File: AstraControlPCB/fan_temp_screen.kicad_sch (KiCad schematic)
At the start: 23 parts, among them CN4 4P JST ZH, CN5 4P JST ZH, CN6 4P JST ZH

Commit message: update
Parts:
- removed R26, R27, R33, R34: 0, LiveAstra:R_0805_2012Metric_Pad1.20x1.40mm_HandSolder, symbol LiveAstra:R_0Ohm_0805_125mW
- added R26, R27, R33, R34: DNP, LiveAstra:R_0805_2012Metric_Pad1.20x1.40mm_HandSolder, symbol LiveAstra:R_DNP_0805
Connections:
- net +3V3: now also R26.2, R27.2, R33.2, R34.2
- net SCREEN_I2C_SCL: now also R27.1
- net SCREEN_I2C_SDA: now also R34.1
- net TEMP_I2C_SCL: now also R26.1
- net TEMP_I2C_SDA: now also R33.1

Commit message: Fixed fab layer
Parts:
- R26, R27, R33, R34: footprint LiveAstra:R_0805_2012Metric_Pad1.20x1.40mm_HandSolder -> LiveAstra:R_DNP_0805_2012Metric_Pad1.20x1.40mm_HandSolder
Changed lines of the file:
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@@
 			)
 		)
-		(property "Footprint" "LiveAstra:R_0805_2012Metric_Pad1.20x1.40mm_HandSolder"
+		(property "Footprint" "LiveAstra:R_DNP_0805_2012Metric_Pad1.20x1.40mm_HandSolder"
 			(at 228.6 152.4 0)
 			(effects
@@
 			)
 		)
-		(property "Footprint" "LiveAstra:R_0805_2012Metric_Pad1.20x1.40mm_HandSolder"
+		(property "Footprint" "LiveAstra:R_DNP_0805_2012Metric_Pad1.20x1.40mm_HandSolder"
 			(at 137.16 96.52 0)
 			(effects
@@
 			)
 		)
-		(property "Footprint" "LiveAstra:R_0805_2012Metric_Pad1.20x1.40mm_HandSolder"
+		(property "Footprint" "LiveAstra:R_DNP_0805_2012Metric_Pad1.20x1.40mm_HandSolder"
 			(at 228.6 101.6 0)
 			(effects
@@
 			)
 		)
-		(property "Footprint" "LiveAstra:R_0805_2012Metric_Pad1.20x1.40mm_HandSolder"
+		(property "Footprint" "LiveAstra:R_DNP_0805_2012Metric_Pad1.20x1.40mm_HandSolder"
 			(at 137.16 147.32 0)
 			(effects

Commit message: Updates
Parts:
- renumbered C22 to C23, INF6 to INF8, R23 to R24, R24 to R25, R25 to R26, R26 to R27, R27 to R28, R28 to R29, R29 to R30, R30 to R31, R31 to R32, R32 to R33, R33 to R34, R34 to R35

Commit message: Added MFN MPR to each components for eurocircuits
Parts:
- C23: MFN (none) -> Samsung Electro-Mechanics; MPN (none) -> CL21C101JBANNNC
- CN4, CN5, CN6: MFN (none) -> JST; MPN (none) -> B4B-ZR-3.4(LF)(SN)
- R24, R25, R32, R33: MFN (none) -> UNI-ROYAL(Uniroyal Elec); MPN (none) -> 0402WGF5101TCE
- R26, R29: MFN (none) -> UNI-ROYAL(Uniroyal Elec); MPN (none) -> 0805W8F0000T5E
- R30: MFN (none) -> UNI-ROYAL(Uniroyal Elec); MPN (none) -> 0402WGF1002TCE
- R31: MFN (none) -> UNI-ROYAL(Uniroyal Elec); MPN (none) -> 0805W8F3301T5E
- TP33, TP34, TP35, TP36, TP37, TP38: MFN (none) -> ronghe; MPN (none) -> RH-5000

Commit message: Update schematic titles, templates
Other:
- title: AstraControl - Root -> AstraControl - Fan Temperature Screen
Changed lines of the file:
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@@
 	(paper "A4")
 	(title_block
-		(title "AstraControl - Root")
+		(title "AstraControl - Fan Temperature Screen")
 		(date "2024-08-26")
 		(rev "A")

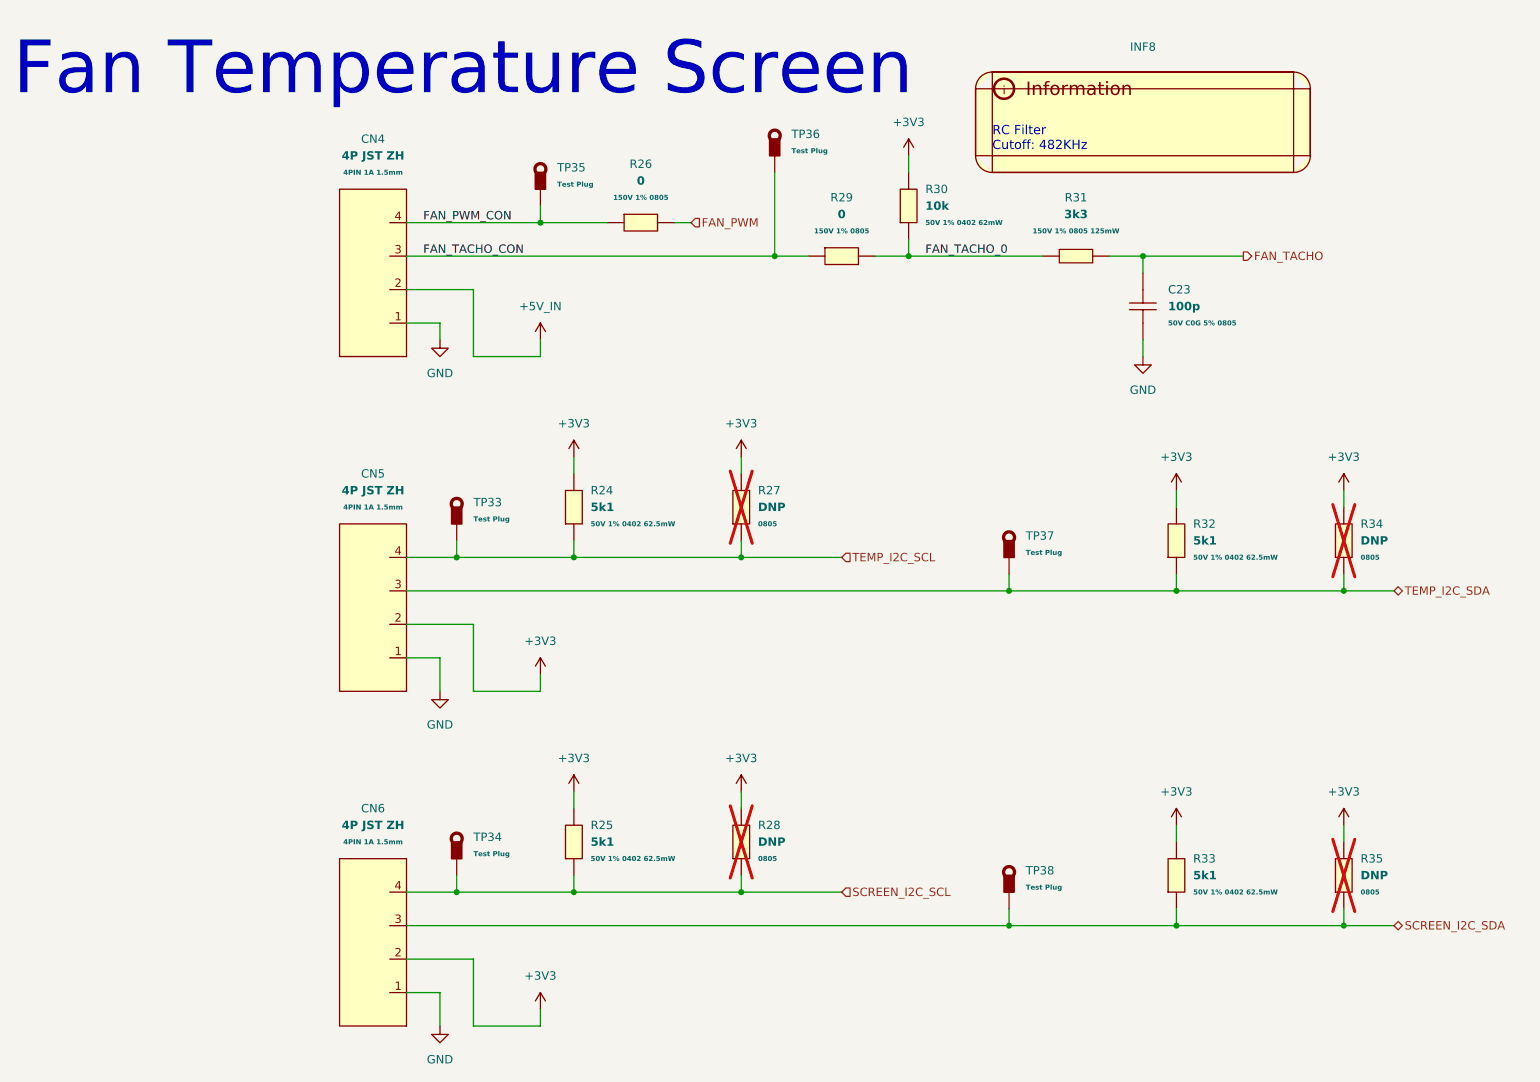
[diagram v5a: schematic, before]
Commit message: Update to new rs485 chip, use 2 bit 5v gpio
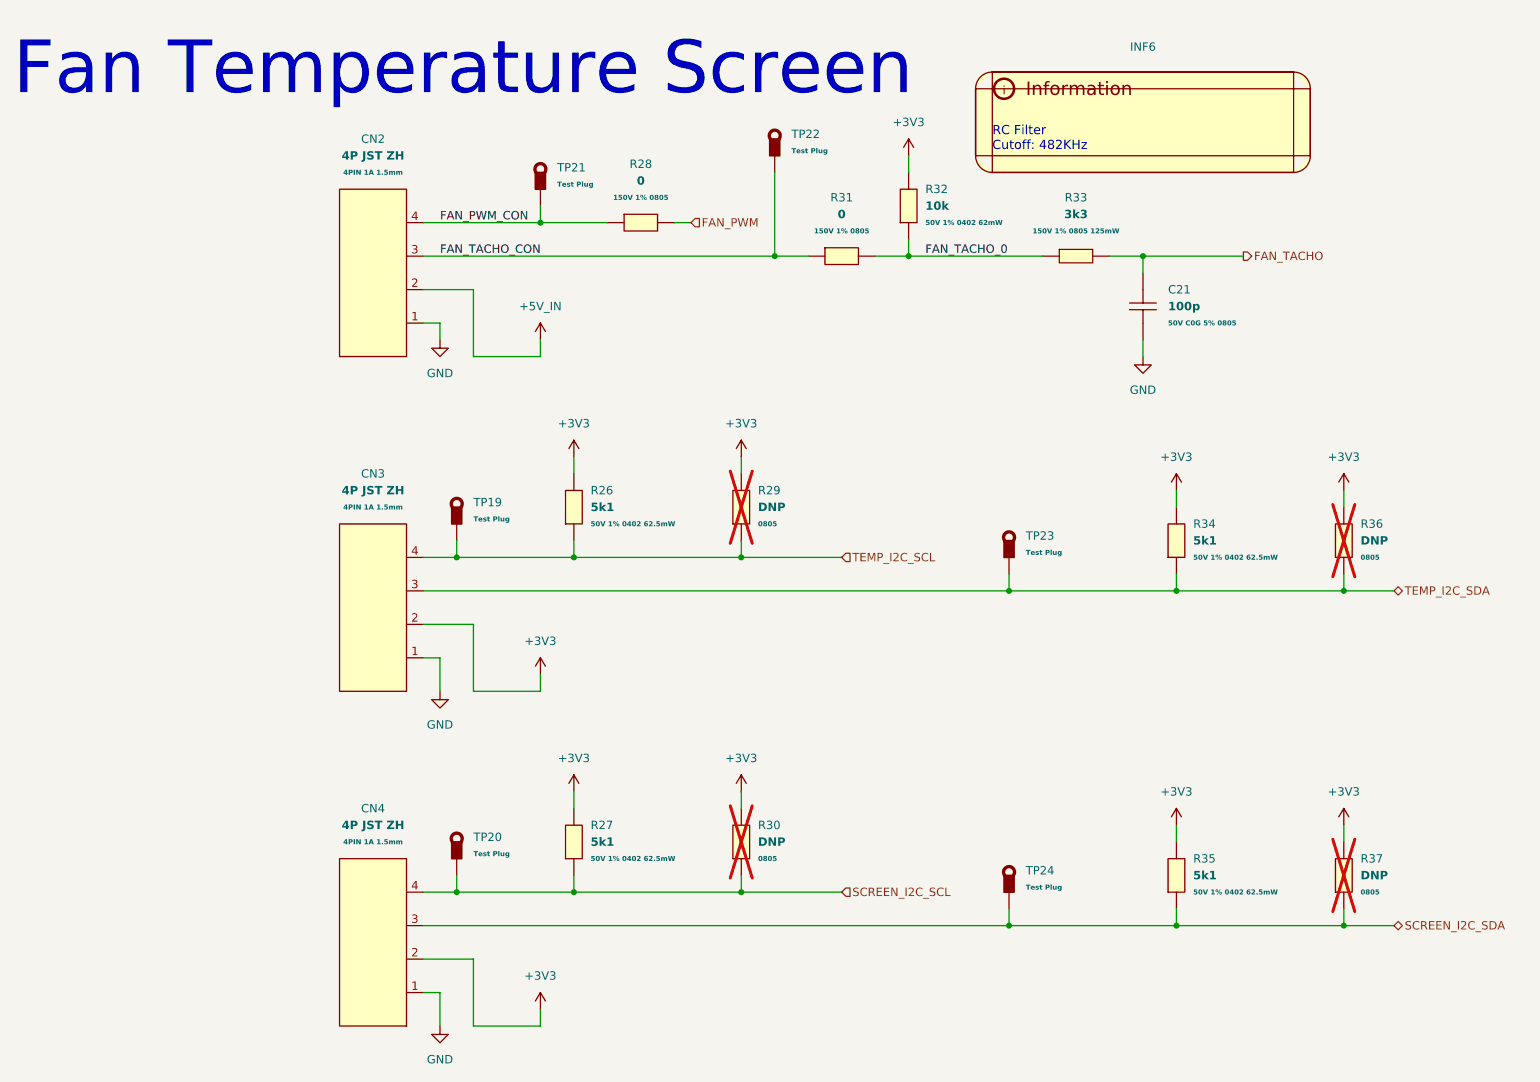
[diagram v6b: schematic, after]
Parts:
- renumbered C23 to C21, CN4 to CN2, CN5 to CN3, CN6 to CN4, INF8 to INF6, R24 to R26, R25 to R27, R26 to R28, R27 to R29, R28 to R30, R29 to R31, R30 to R32, R31 to R33, R32 to R34, R33 to R35, R34 to R36, R35 to R37, TP33 to TP19, TP34 to TP20, TP35 to TP21, TP36 to TP22, TP37 to TP23, TP38 to TP24
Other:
- moved on the sheet: CN2, CN3, CN4

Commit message: New inductor that is in stock, updated rs485 ic layout to put caps closer
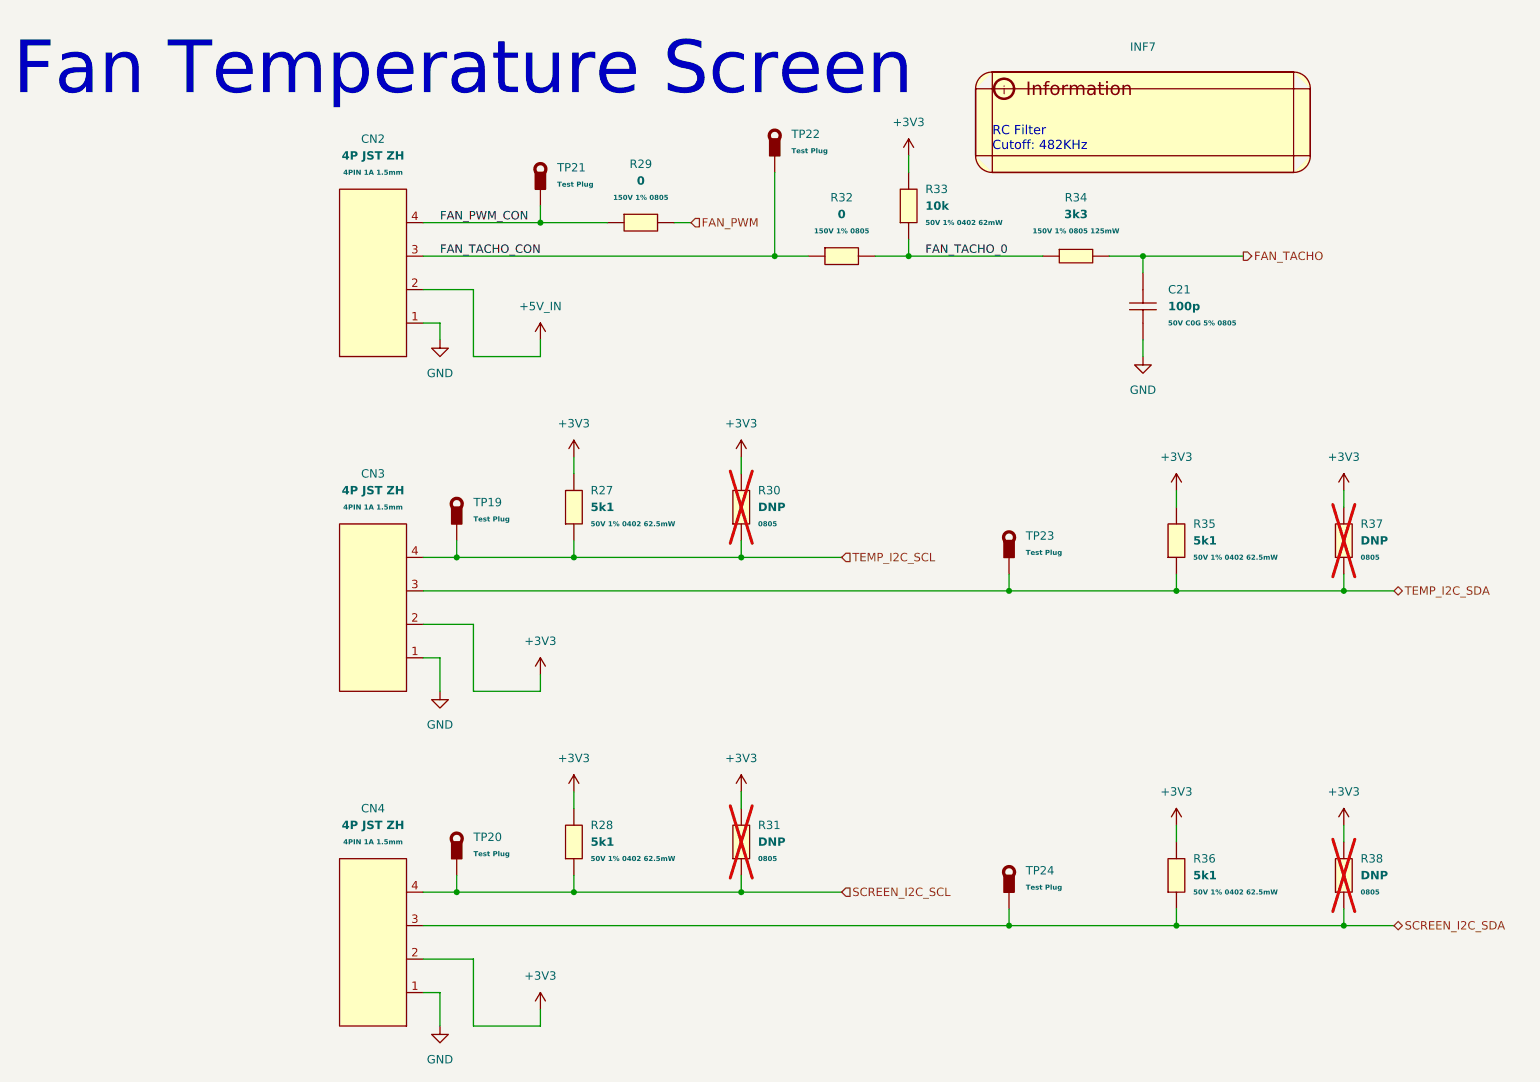
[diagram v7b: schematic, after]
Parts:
- renumbered INF6 to INF7, R26 to R27, R27 to R28, R28 to R29, R29 to R30, R30 to R31, R31 to R32, R32 to R33, R33 to R34, R34 to R35, R35 to R36, R36 to R37, R37 to R38

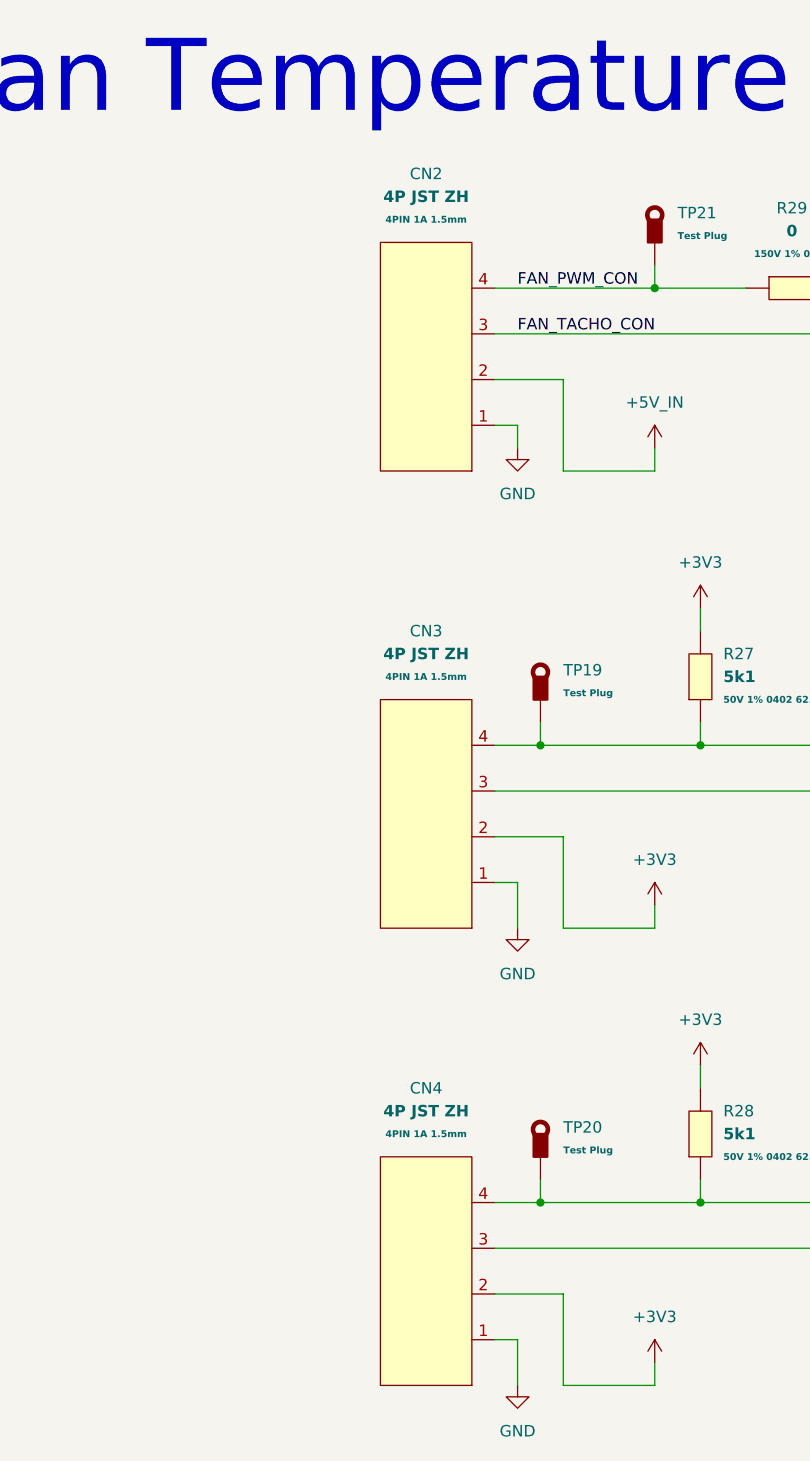
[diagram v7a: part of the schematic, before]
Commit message: Updated to JST SH, 3A diode for USB, added extra 2P VH
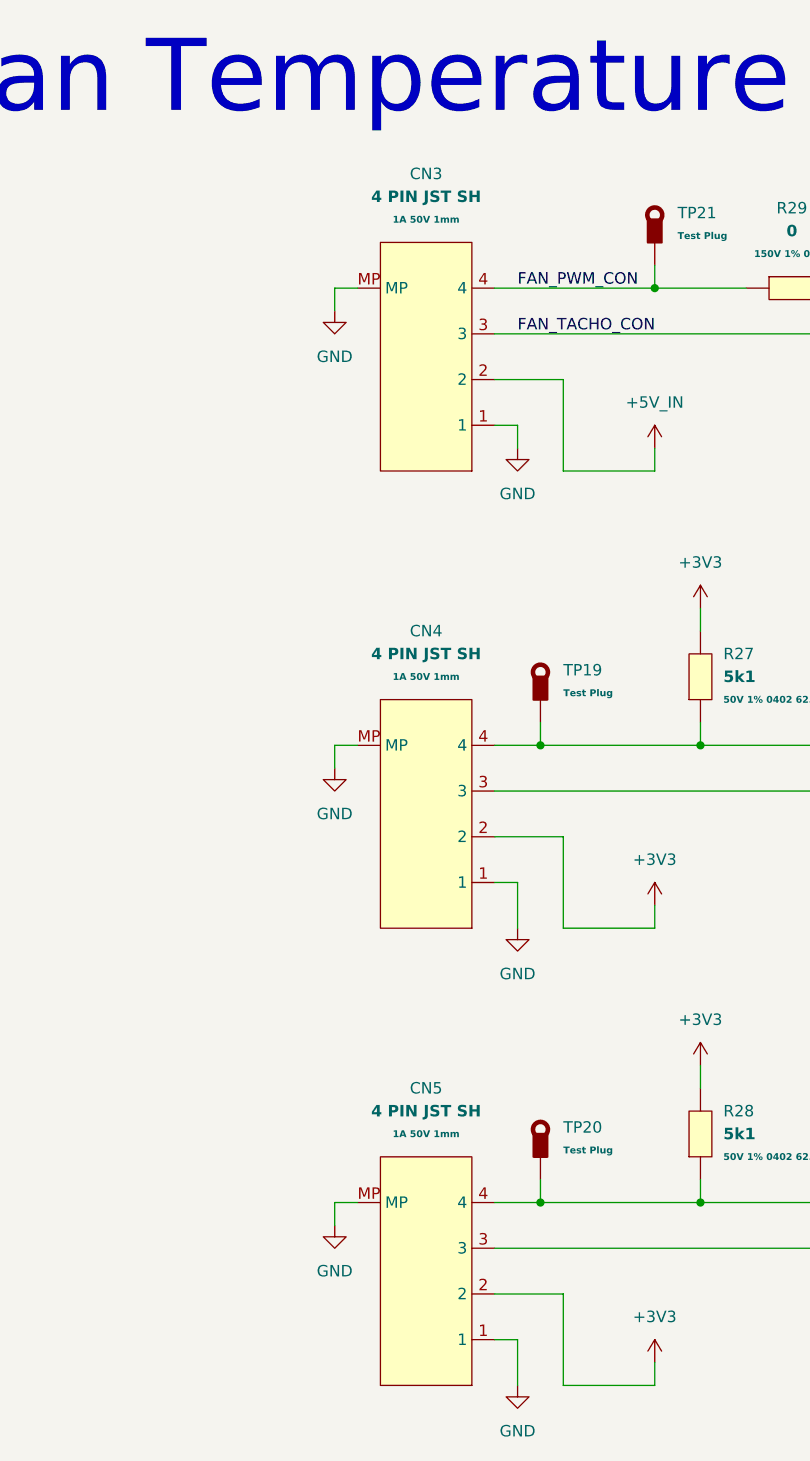
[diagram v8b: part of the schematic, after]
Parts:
- removed CN2, CN3, CN4: 4P JST ZH, LiveAstra:JST_ZH_B4B-ZR_1x04_P1.50mm_Vertical, symbol LiveAstra:JST_ZH_4PIN_1A_50V
- added CN3, CN4, CN5: 4 PIN JST SH, LiveAstra:JST_SH_1x04_P1.00mm_Vertical, symbol LiveAstra:JST_SH_4PIN_1A_50V
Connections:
- net +3V3: now also CN4.2, CN5.2
- net +5V_IN: now also CN3.2
- net FAN_PWM_CON: now also CN3.4
- net FAN_TACHO_CON: now also CN3.3
- net GND: now also CN3.1, CN3.MP, CN4.1, CN4.MP, CN5.1, CN5.MP
- net SCREEN_I2C_SCL: now also CN5.4
- net SCREEN_I2C_SDA: now also CN5.3
- net TEMP_I2C_SCL: now also CN4.4
- net TEMP_I2C_SDA: now also CN4.3
